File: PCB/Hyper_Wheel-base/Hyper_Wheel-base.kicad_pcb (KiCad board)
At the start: 4 copper layers, 81.9 x 68 mm, 77 parts, among them J2 LIPO, J3 USB4215-03-A, SW1 SW_Push, SW2 SW_Push, U1 CSD85301Q2, U10 TPS22916CNYFPR, U11 TPD2EUSB30ADRTR, U12 TPS22916CNYFPR, U13 AS5600L-ASOM, U14 DRV5032FCDBZR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

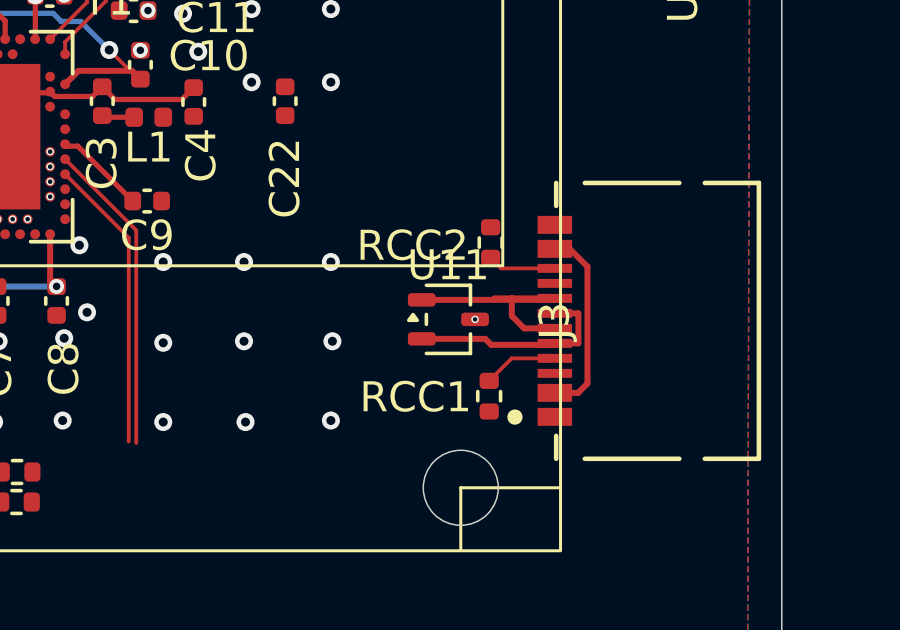
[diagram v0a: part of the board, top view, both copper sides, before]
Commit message: Missing TVS Diode places
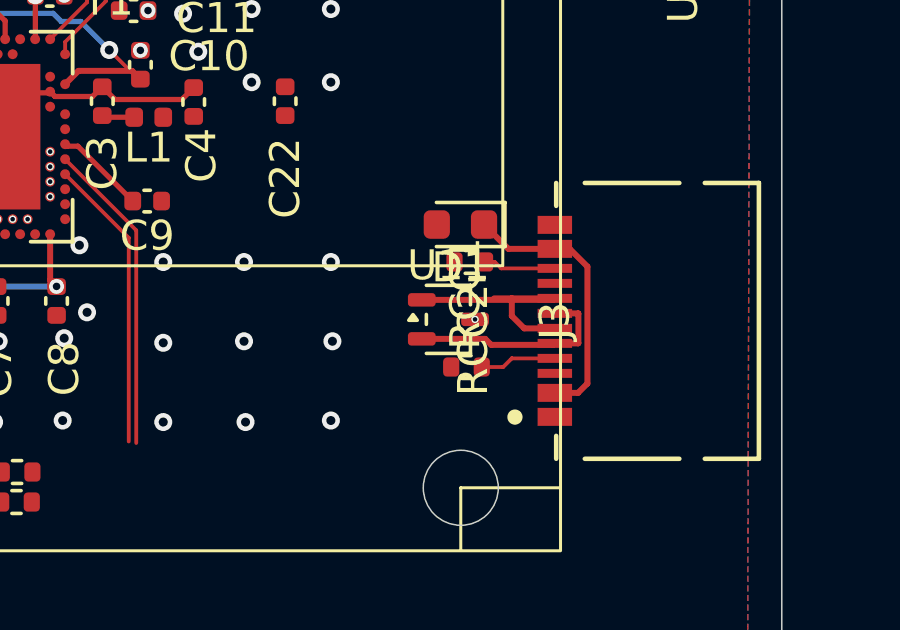
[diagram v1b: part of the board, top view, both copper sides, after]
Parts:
- added D1: D_TVS, Diode_SMD:D_0603_1608Metric, F.Cu at (246.3, 67.8)
- moved RCC1 1.23 mm to (246.5, 72.5), turned to 180 degrees
- moved RCC2 0.95 mm to (246.6, 69.0), turned to 180 degrees
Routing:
- net /USB Vbus: track 14.5 -> 17.2 mm

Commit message: Updated work on antenna, And adjusted log structure
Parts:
- U17: footprint Hyper_Wheel:2450AT07A0100T_JOT -> Hyper_Wheel:2450AT07A0100T_JOT+Keepout
- moved U17 1.34 mm to (255.1, 59.7), turned to -90 degrees
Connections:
- net /MCU_RF/PWR (page 3)/To_Antenna renamed /AntFeed

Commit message: 4-6 progress update
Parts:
- moved U17 5.71 mm to (255.1, 54.0)
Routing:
- net /AntFeed: track 0.00 -> 1.56 mm
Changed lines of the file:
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@@
 	(footprint "Hyper_Wheel:2450AT07A0100T_JOT+Keepout"
 		(layer "F.Cu")
-		(at 255.05 59.665 -90)
+		(at 255.05 53.95 -90)
 		(tags "2450AT07A0100T ")
 		(property "Reference" "U17"
@@
 			(polygon
 				(pts
-					(xy 255.2 58.715) (xy 255.2 63.715) (xy 253 63.715) (xy 253 58.715) (xy 254.2 58.715) (xy 254.2 60.215)
-					(xy 254.9 60.215) (xy 254.9 58.715)
+					(xy 255.2 53) (xy 255.2 58) (xy 253 58) (xy 253 53) (xy 254.2 53) (xy 254.2 54.5) (xy 254.9 54.5)
+					(xy 254.9 53)
 				)
 			)
@@
 			(polygon
 				(pts
-					(xy 255.2 59.615) (xy 255.9 59.615) (xy 255.9 58.715) (xy 256 58.715) (xy 256 63.715) (xy 255.9 63.715)
-					(xy 255.9 59.715) (xy 255.2 59.715)
+					(xy 255.2 53.9) (xy 255.9 53.9) (xy 255.9 53) (xy 256 53) (xy 256 58) (xy 255.9 58) (xy 255.9 54)
+					(xy 255.2 54)
 				)
 			)
@@
 			(polygon
 				(pts
-					(xy 256 58.715) (xy 253 58.715) (xy 253 63.715) (xy 256 63.715)
+					(xy 256 53) (xy 253 53) (xy 253 58) (xy 256 58)
 				)
 			)
@@
 		(net "Net-(J3-CC2)")
 	)
+	(segment
+		(start 254.75 54.275)
+		(end 254.75 53.460196)
+		(width 0.127)
+		(layer "F.Cu")
+		(net "/AntFeed")
+	)
+	(segment
+		(start 254.75 53.460196)
+		(end 254.226304 52.9365)
+		(width 0.127)
+		(layer "F.Cu")
+		(net "/AntFeed")
+	)
 	(zone
 		(net "GND")
@@
 		(priority 1)
 		(connect_pads
-			(clearance 0.5)
+			(clearance 0.127)
 		)
 		(min_thickness 0.25)

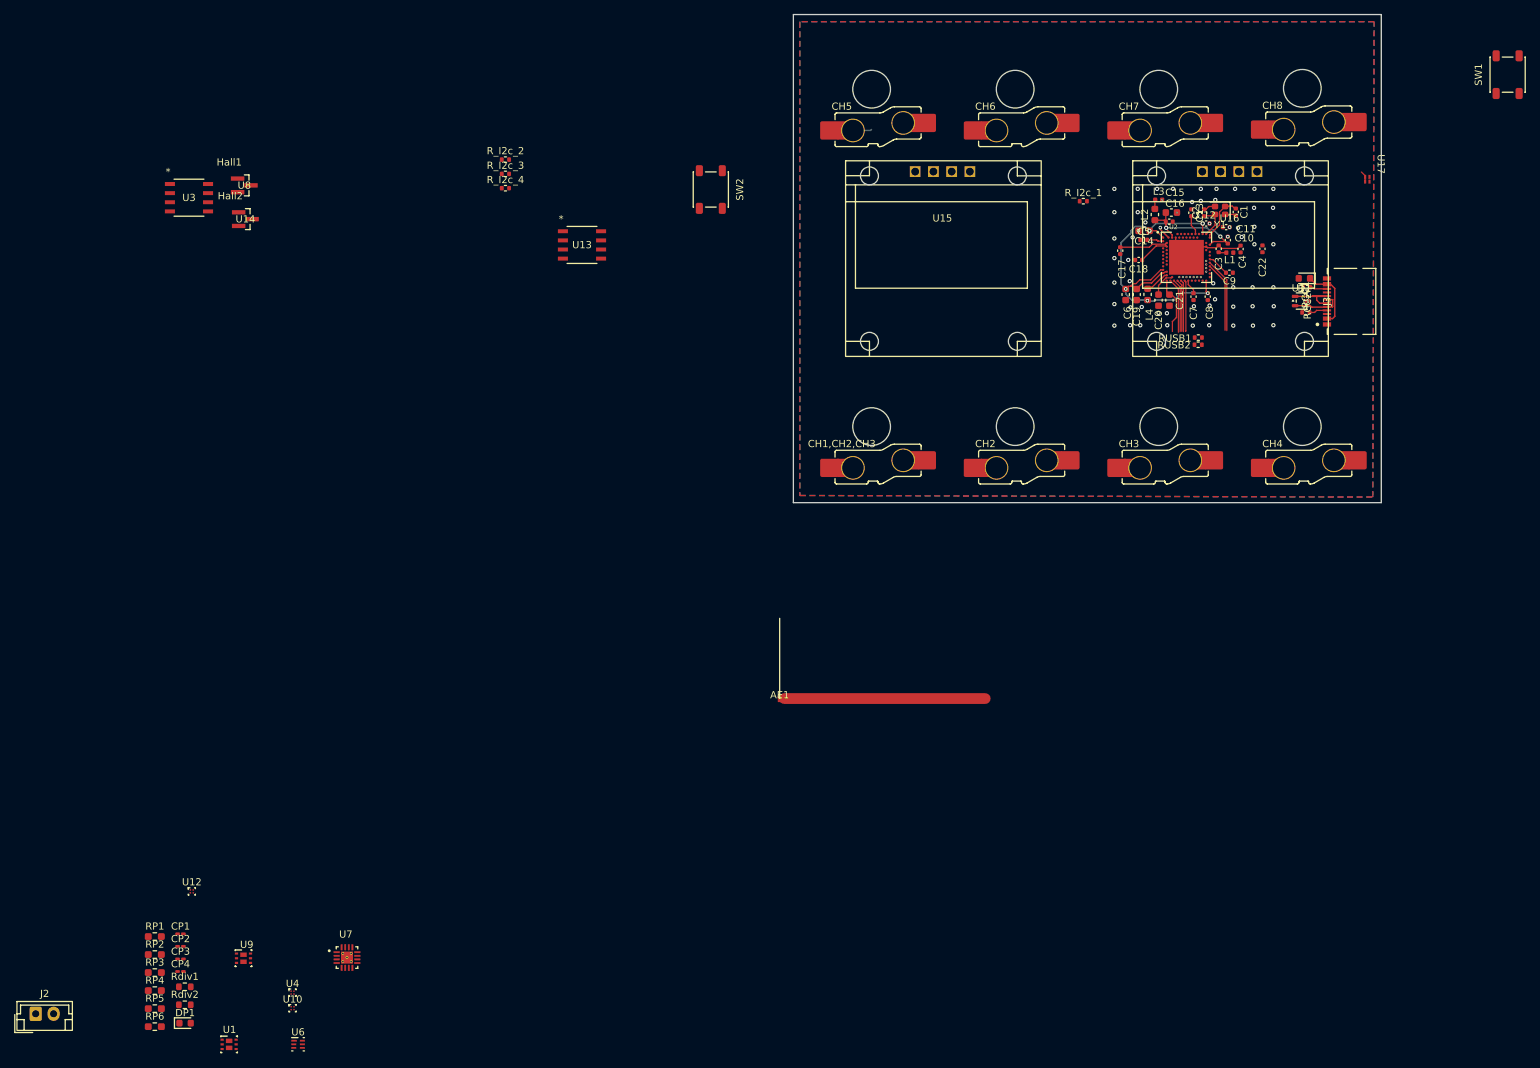
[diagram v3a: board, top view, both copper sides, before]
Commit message: Main board nearing RevA completion
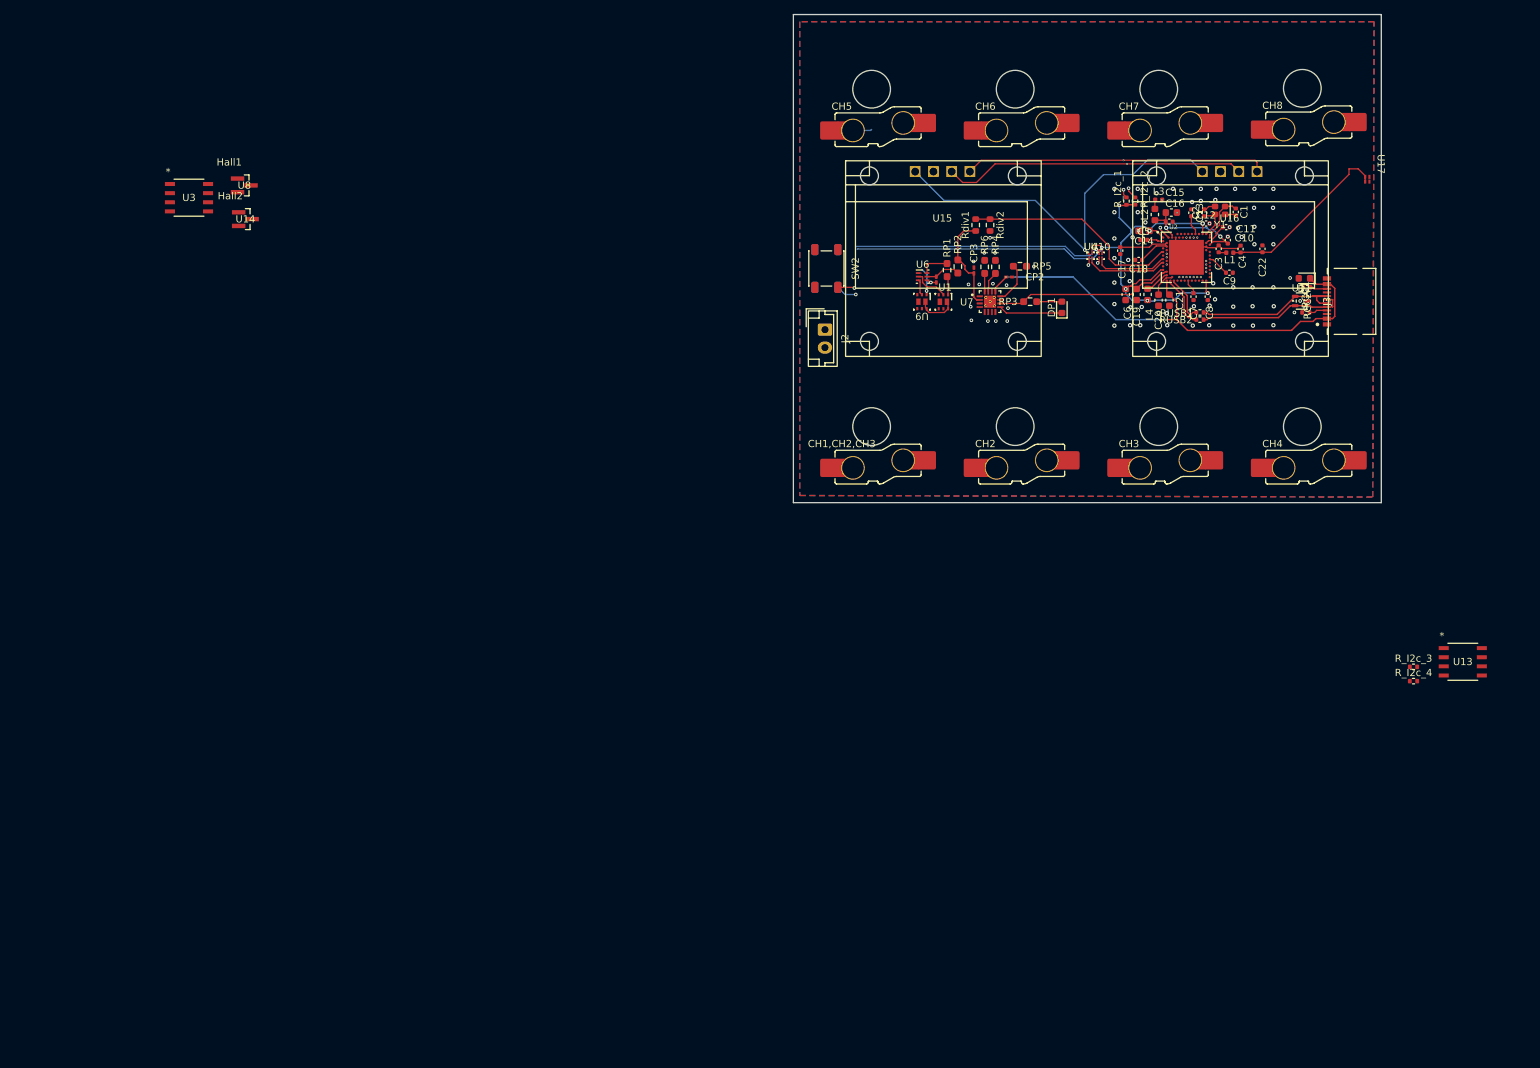
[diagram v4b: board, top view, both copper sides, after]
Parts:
- removed AE1: Antenna, Hyper_Wheel:28mm Linear ANT
- removed CP4: 1u, Capacitor_SMD:C_0201_0603Metric_Pad0.64x0.40mm_HandSolder
- removed U12: TPS22916CNYFPR, Hyper_Wheel:TPS22916-YFP0004ABAB
- SW1: moved to B.Cu
- moved RP5 158.8 mm to (206.7, 66.1)
- moved DP1 157.7 mm to (212.5, 71.8), turned to 90 degrees
- moved RP6 156.7 mm to (201.8, 66.2), turned to 90 degrees
- moved Rdiv2 156.1 mm to (202.5, 60.3), turned to -90 degrees
- moved RP4 154.5 mm to (203.2, 66.2), turned to -90 degrees
- moved U10 153.8 mm to (217.9, 64.6)
- moved RP3 153.6 mm to (208.1, 71.0)
- moved Rdiv1 153.0 mm to (200.5, 60.3), turned to 90 degrees
- moved U4 151.3 mm to (216.5, 64.6)
- moved CP2 148.4 mm to (205.2, 67.6), turned to 180 degrees
- moved RP2 147.3 mm to (198.0, 66.1), turned to 90 degrees
- moved CP3 146.3 mm to (200.2, 66.7), turned to 90 degrees
- moved J2 145.5 mm to (179.5, 74.9), turned to -90 degrees
- moved RP1 144.2 mm to (196.5, 66.6), turned to -90 degrees
- moved R_I2c_3 143.9 mm to (261.5, 121.9)
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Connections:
- net Net-(U2A-D+) renamed /D2+
- net Net-(U2A-D-) renamed /D2-
- CH1,CH2,CH3 pad 1: /Peripherals/Key1 -> /Key1
- CH2 pad 1: /Peripherals/Key2 -> /Key2
- CH3 pad 1: /Peripherals/Key3 -> /Key3
- CH4 pad 1: /Peripherals/Key4 -> /Key4
- CH5 pad 1: /Peripherals/Key5 -> /Key5
- CH6 pad 1: /Peripherals/Key6 -> /Key6
- CH7 pad 1: /Peripherals/Key7 -> /Key7
- CH8 pad 1: /Peripherals/Key8 -> /Key8
- CP3 pad 1: GND -> /Power Handling/Cell+
- J2 pad 1: GND -> /Power Handling/Cell+
- RP2 pad 2: GND -> /Power Handling/Cell+
- Rdiv1 pad 1: GND -> /Power Handling/Cell+
- SW2 pad 1: unconnected-(SW2-Pad1) -> /Switch
- U1 pad 7: Net-(U1A-D1-Pad7) -> Net-(U1A-D1-Pad6)
- U2 pad AC15: unconnected-(U2A-P0.19-PadAC15) -> /Switch
- U2 pad N1: unconnected-(U2A-P0.08-PadN1) -> /Load1 CTRL
- U2 pad R1: unconnected-(U2A-P1.09-PadR1) -> /Load2 CTRL
- U2 pad R24: /Load2 CTRL -> unconnected-(U2A-P1.06-PadR24)
- U2 pad U24: /Load1 CTRL -> unconnected-(U2A-P1.04-PadU24)
- U7 pad 2: GND -> /Power Handling/Cell+
- U9 pad 7: Net-(U1A-D1-Pad7) -> Net-(U1A-D1-Pad6)
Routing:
- net /I2C_1_SDA: track 0.00 -> 62.1 mm, vias 0 -> 3
- net /I2C_1_SCL: track 0.00 -> 60.8 mm, vias 0 -> 3
- net /Switch: track 0.00 -> 57.2 mm, vias 0 -> 2
- net /Key1: track 9.16 -> 65.9 mm
- net /Load2 V: track 0.00 -> 55.9 mm, vias 0 -> 1
- net /Key5: track 0.00 -> 50.6 mm, vias 0 -> 1
- net /USB Vbus: track 17.2 -> 66.5 mm, vias 0 -> 2
- net Net-(U2A-P0.18/~{RESET}): track 6.92 -> 55.5 mm, vias 1 -> 2
- net 3.3V_Regulated: track 46.9 -> 95.0 mm, vias 5 -> 7
- net /Key2: track 9.78 -> 49.0 mm
- net /Load1 V: track 0.00 -> 35.3 mm, vias 0 -> 1
- net /Key8: track 0.00 -> 33.8 mm, vias 0 -> 1
- net /Key6: track 0.00 -> 31.0 mm, vias 0 -> 1
- net /Cell_monitor: track 0.00 -> 30.6 mm
- net /Key4: track 11.0 -> 41.3 mm
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
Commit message: power plane added,  passes Peer review
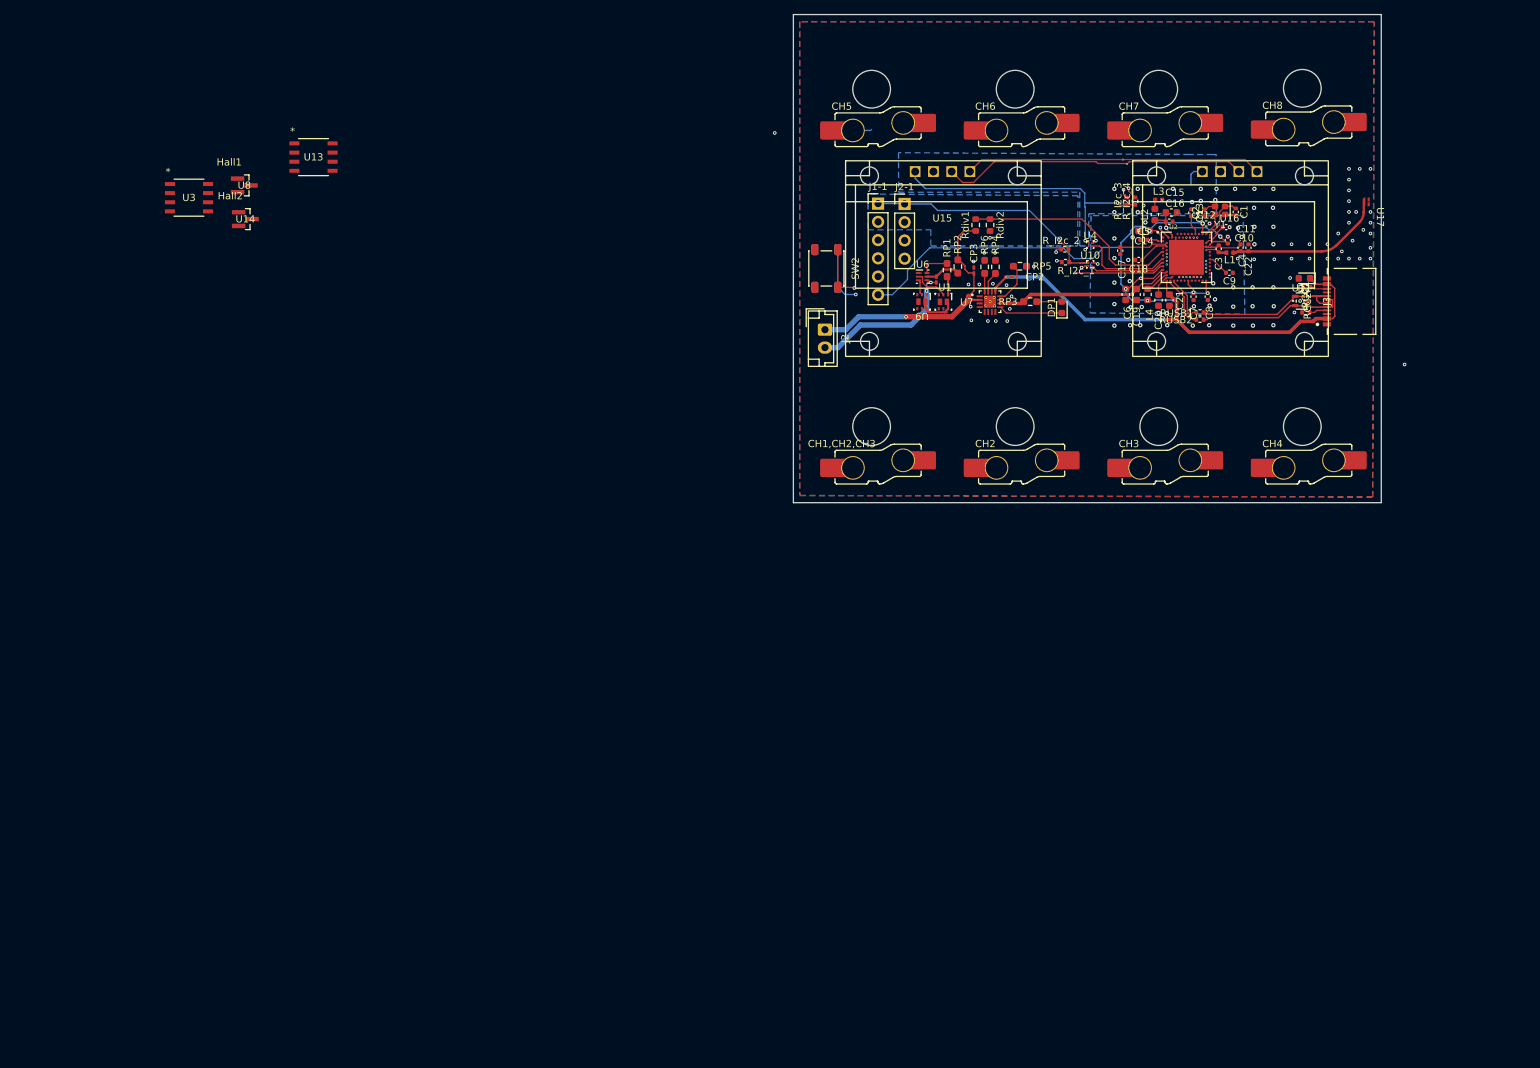
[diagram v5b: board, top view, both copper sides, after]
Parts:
- added J1-1: Conn_01x06_Socket, Connector_PinHeader_2.54mm:PinHeader_1x06_P2.54mm_Vertical, F.Cu at (186.9, 57.3)
- added J2-1: Conn_01x04_Socket, Connector_PinHeader_2.54mm:PinHeader_1x04_P2.54mm_Vertical, F.Cu at (190.6, 57.4)
- moved U13 174.9 mm to (108.3, 50.9)
- moved R_I2c_4 77.3 mm to (222.7, 57.0), turned to 90 degrees
- moved R_I2c_3 76.2 mm to (221.5, 57.0), turned to 90 degrees
- moved R_I2c_1 12.0 mm to (213.0, 65.5), turned to 180 degrees
- moved R_I2c_2 11.9 mm to (212.9, 63.7), turned to 180 degrees
- moved C22 1.95 mm to (238.5, 63.5)
- moved U17 1.94 mm to (254.9, 52.0)
- moved U10 1.88 mm to (216.4, 65.8)
- moved U4 1.55 mm to (216.4, 63.0)
- moved C4 0.19 mm to (237.4, 63.5)
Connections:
- R_I2c_1 pad 1: 3.3V_Regulated -> /Load1 V
- R_I2c_2 pad 1: 3.3V_Regulated -> /Load1 V
- R_I2c_3 pad 1: /I2C_2_SDA -> /Load2 V
- R_I2c_3 pad 2: 3.3V_Regulated -> /I2C_2_SDA
- R_I2c_4 pad 1: /I2C_2_SCL -> /Load2 V
- R_I2c_4 pad 2: 3.3V_Regulated -> /I2C_2_SCL
- U13 pad 2: /Load1 V -> Net-(JJ2-2-Pin_1)
- U13 pad 4: GND -> Net-(JJ2-2-Pin_2)
- U13 pad 6: /I2C_2_SDA -> Net-(JJ2-2-Pin_4)
- U13 pad 7: /I2C_2_SCL -> Net-(JJ2-2-Pin_3)
- U14 pad 1: 3.3V_Regulated -> /Peripherals/OB-3.3v
- U14 pad 2: /Hall_1 -> /Peripherals/OB-Hall
- U14 pad 3: GND -> /Peripherals/OB-GND
- U15 pad 3: /I2C_1_SCL -> /I2C_2_SCL
- U15 pad 4: /I2C_1_SDA -> /I2C_2_SDA
- U16 pad 3: /I2C_1_SCL -> /I2C_2_SCL
- U16 pad 4: /I2C_1_SDA -> /I2C_2_SDA
- U2 pad AD18: /I2C_2_SDA -> unconnected-(U2A-P0.22-PadAD18)
- U2 pad AD20: /I2C_2_SCL -> unconnected-(U2A-P0.24-PadAD20)
- U2 pad K2: /I2C_1_SCL -> /I2C_2_SCL
- U2 pad M2: /I2C_1_SDA -> /I2C_2_SDA
- U2 pad N1: /Load1 CTRL -> /Load2 CTRL
- U2 pad P2: unconnected-(U2A-P1.08-PadP2) -> /I2C_1_SCL
- U2 pad R1: /Load2 CTRL -> /Load1 CTRL
- U2 pad T2: unconnected-(U2A-P0.11-PadT2) -> /I2C_1_SDA
- U3 pad 2: /Load1 V -> /Peripherals/OB-Load
- U3 pad 4: GND -> /Peripherals/OB-GND
- U3 pad 6: /I2C_1_SDA -> /Peripherals/OB-SDA
- U3 pad 7: /I2C_1_SCL -> /Peripherals/OB-SCL
- U8 pad 1: 3.3V_Regulated -> /Peripherals/OB-3.3v
- U8 pad 2: /Hall_1 -> /Peripherals/OB-Hall
- U8 pad 3: GND -> /Peripherals/OB-GND
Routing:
- net /I2C_2_SDA: track 0.00 -> 61.5 mm, vias 0 -> 3
- net /I2C_2_SCL: track 0.00 -> 61.3 mm, vias 0 -> 3
- net /Hall_1: track 0.00 -> 40.3 mm, vias 0 -> 1
- net /Power Handling/Cell+: track 13.6 -> 36.7 mm, vias 0 -> 1
- net /I2C_1_SDA: track 62.1 -> 42.5 mm, vias 3 -> 2
- net /I2C_1_SCL: track 60.8 -> 43.2 mm, vias 3 -> 2
- net /Power Handling/Cell-: track 5.98 -> 22.6 mm
- net /Load2 V: track 55.9 -> 43.1 mm, vias 1 -> 2
- net 3.3V_Regulated: track 95.0 -> 87.4 mm, vias 7 -> 9
- net /Switch: track 57.2 -> 62.7 mm
- net Net-(U2A-P0.18/~{RESET}): track 55.5 -> 60.7 mm
- net /AntFeed: track 24.9 -> 22.5 mm
- net ChargerOUT: track 25.2 -> 27.2 mm
- net Net-(U2B-ANT): track 1.09 -> 3.02 mm
- net /Load2 CTRL: track 11.6 -> 13.2 mm
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- added copper zone on B.Cu, net /Load1 V
- added copper zone on B.Cu, net /Load2 V
- added copper zone on B.Cu, net 3.3V_Regulated
